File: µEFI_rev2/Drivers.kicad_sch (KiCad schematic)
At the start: 28 parts, among them Q1 ISL9V5045S3ST, Q2 ISL9V5045S3ST, Q3 ISL9V5045S3ST, Q4 ISL9V5045S3ST

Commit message: uEFI v2 beta release
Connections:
- net CONN_1 renamed M4
- net CONN_2 renamed L3
- net CONN_21 renamed M3
- net CONN_22 renamed L4
- net CONN_41 renamed L2
- net CONN_42 renamed M2
- net CONN_61 renamed L1
- net CONN_62 renamed M1
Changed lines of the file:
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@@
     (effects (font (size 1.27 1.27)) (justify right bottom))
   )
-  (global_label "CONN_62" (shape input) (at 90.17 59.69 0)
-    (effects (font (size 1.27 1.27)) (justify left))
-    (property "Intersheet References" "${INTERSHEET_REFS}" (id 0) (at 0 0 0)
-      (effects (font (size 1.27 1.27)) hide)
+  (global_label "M1" (shape input) (at 90.17 59.69 0)
+    (effects (font (size 0.889 0.889)) (justify left))
+    (property "Intersheet References" "${INTERSHEET_REFS}" (id 0) (at 93.7217 59.6345 0)
+      (effects (font (size 0.889 0.889)) (justify left) hide)
     )
   )
-  (global_label "CONN_42" (shape input) (at 90.17 85.09 0)
-    (effects (font (size 1.27 1.27)) (justify left))
-    (property "Intersheet References" "${INTERSHEET_REFS}" (id 0) (at 0 0 0)
-      (effects (font (size 1.27 1.27)) hide)
+  (global_label "M2" (shape input) (at 90.17 85.09 0)
+    (effects (font (size 0.889 0.889)) (justify left))
+    (property "Intersheet References" "${INTERSHEET_REFS}" (id 0) (at 93.7217 85.0345 0)
+      (effects (font (size 0.889 0.889)) (justify left) hide)
     )
   )
-  (global_label "CONN_61" (shape input) (at 90.17 110.49 0)
-    (effects (font (size 1.27 1.27)) (justify left))
-    (property "Intersheet References" "${INTERSHEET_REFS}" (id 0) (at 0 0 0)
-      (effects (font (size 1.27 1.27)) hide)
+  (global_label "L1" (shape input) (at 90.17 110.49 0)
+    (effects (font (size 0.889 0.889)) (justify left))
+    (property "Intersheet References" "${INTERSHEET_REFS}" (id 0) (at 93.4253 110.4345 0)
+      (effects (font (size 0.889 0.889)) (justify left) hide)
     )
   )
-  (global_label "CONN_41" (shape input) (at 90.17 134.62 0)
-    (effects (font (size 1.27 1.27)) (justify left))
-    (property "Intersheet References" "${INTERSHEET_REFS}" (id 0) (at 0 0 0)
-      (effects (font (size 1.27 1.27)) hide)
+  (global_label "L2" (shape input) (at 90.17 134.62 0)
+    (effects (font (size 0.889 0.889)) (justify left))
+    (property "Intersheet References" "${INTERSHEET_REFS}" (id 0) (at 93.4253 134.5645 0)
+      (effects (font (size 0.889 0.889)) (justify left) hide)
     )
   )
-  (global_label "CONN_21" (shape input) (at 165.1 147.32 0)
+  (global_label "M3" (shape input) (at 165.1 147.32 0)
     (effects (font (size 1.27 1.27)) (justify left))
-    (property "Intersheet References" "${INTERSHEET_REFS}" (id 0) (at 0 0 0)
-      (effects (font (size 1.27 1.27)) hide)
+    (property "Intersheet References" "${INTERSHEET_REFS}" (id 0) (at 170.1741 147.2406 0)
+      (effects (font (size 1.27 1.27)) (justify left) hide)
     )
   )
-  (global_label "CONN_1" (shape input) (at 165.1 149.86 0)
+  (global_label "M4" (shape input) (at 165.1 149.86 0)
     (effects (font (size 1.27 1.27)) (justify left))
-    (property "Intersheet References" "${INTERSHEET_REFS}" (id 0) (at 0 0 0)
-      (effects (font (size 1.27 1.27)) hide)
+    (property "Intersheet References" "${INTERSHEET_REFS}" (id 0) (at 170.1741 149.7806 0)
+      (effects (font (size 1.27 1.27)) (justify left) hide)
     )
   )
-  (global_label "CONN_2" (shape input) (at 165.1 152.4 0)
+  (global_label "L3" (shape input) (at 165.1 152.4 0)
     (effects (font (size 1.27 1.27)) (justify left))
-    (property "Intersheet References" "${INTERSHEET_REFS}" (id 0) (at 0 0 0)
-      (effects (font (size 1.27 1.27)) hide)
+    (property "Intersheet References" "${INTERSHEET_REFS}" (id 0) (at 169.7507 152.3206 0)
+      (effects (font (size 1.27 1.27)) (justify left) hide)
     )
   )
-  (global_label "CONN_22" (shape input) (at 165.1 154.94 0)
+  (global_label "L4" (shape input) (at 165.1 154.94 0)
     (effects (font (size 1.27 1.27)) (justify left))
-    (property "Intersheet References" "${INTERSHEET_REFS}" (id 0) (at 0 0 0)
-      (effects (font (size 1.27 1.27)) hide)
+    (property "Intersheet References" "${INTERSHEET_REFS}" (id 0) (at 169.7507 154.8606 0)
+      (effects (font (size 1.27 1.27)) (justify left) hide)
     )
   )

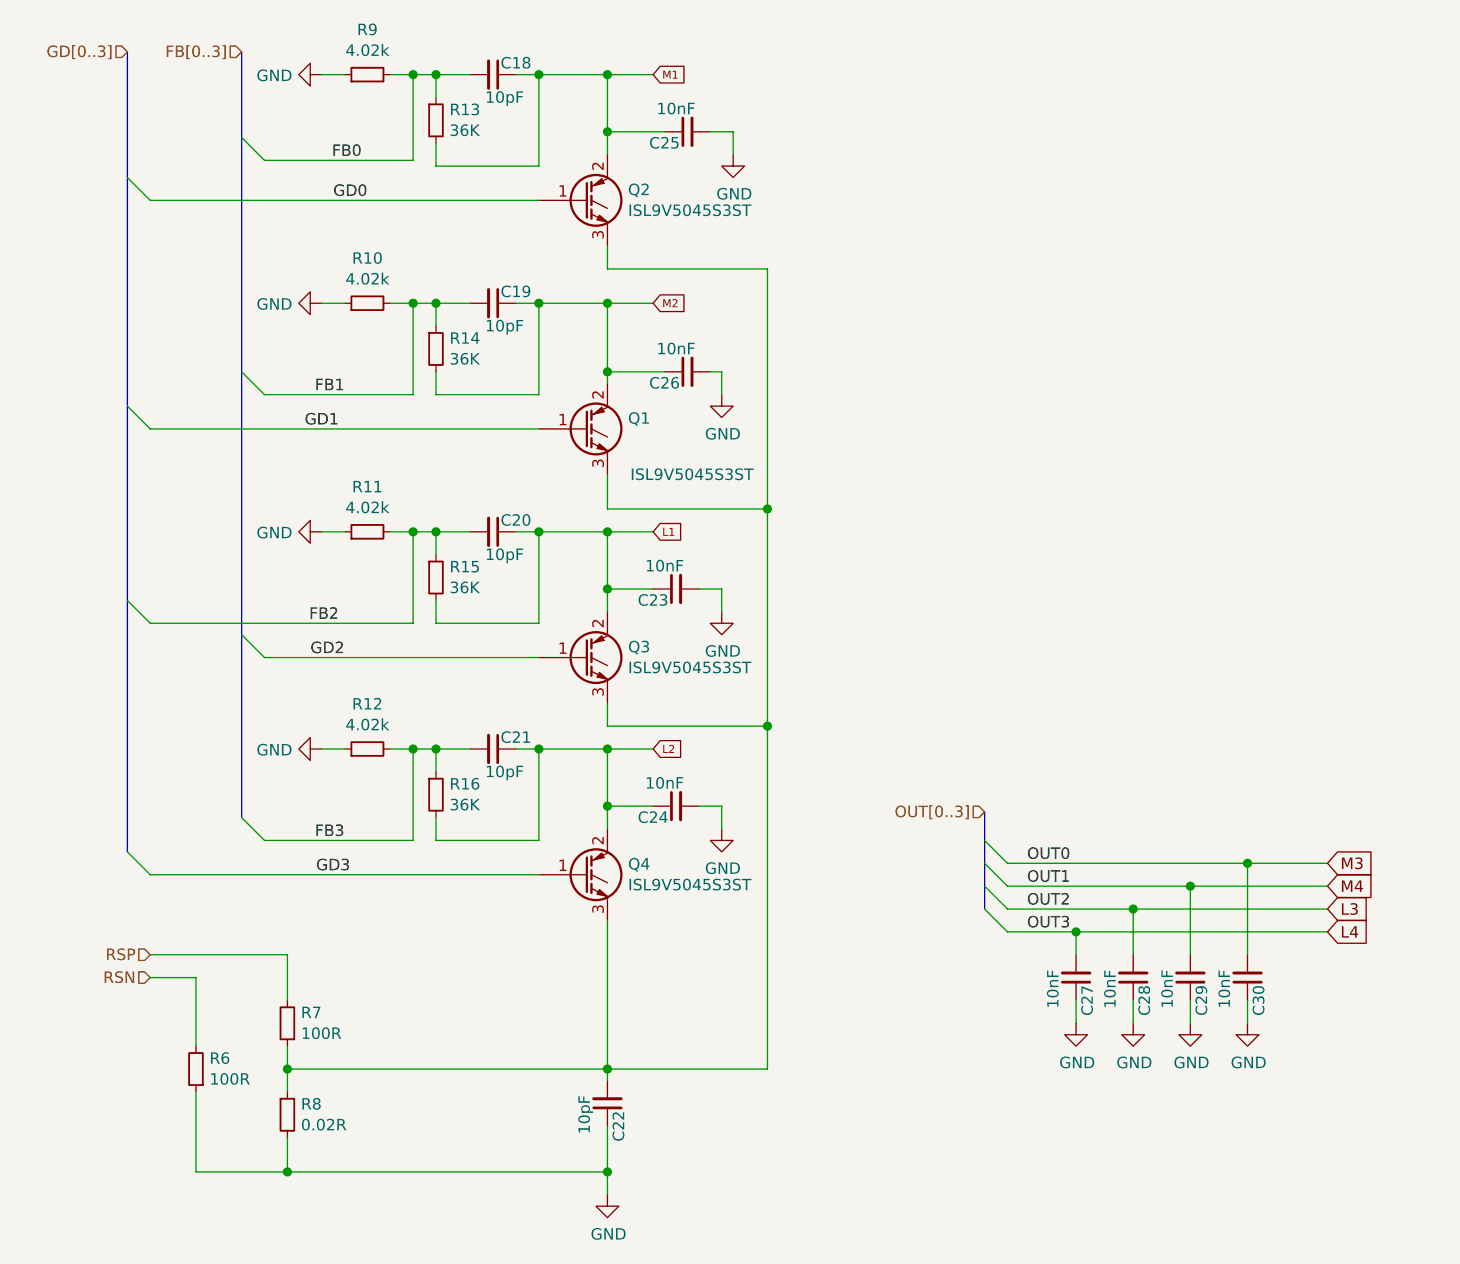
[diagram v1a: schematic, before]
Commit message: bump to kicad 6, init uEFI v3
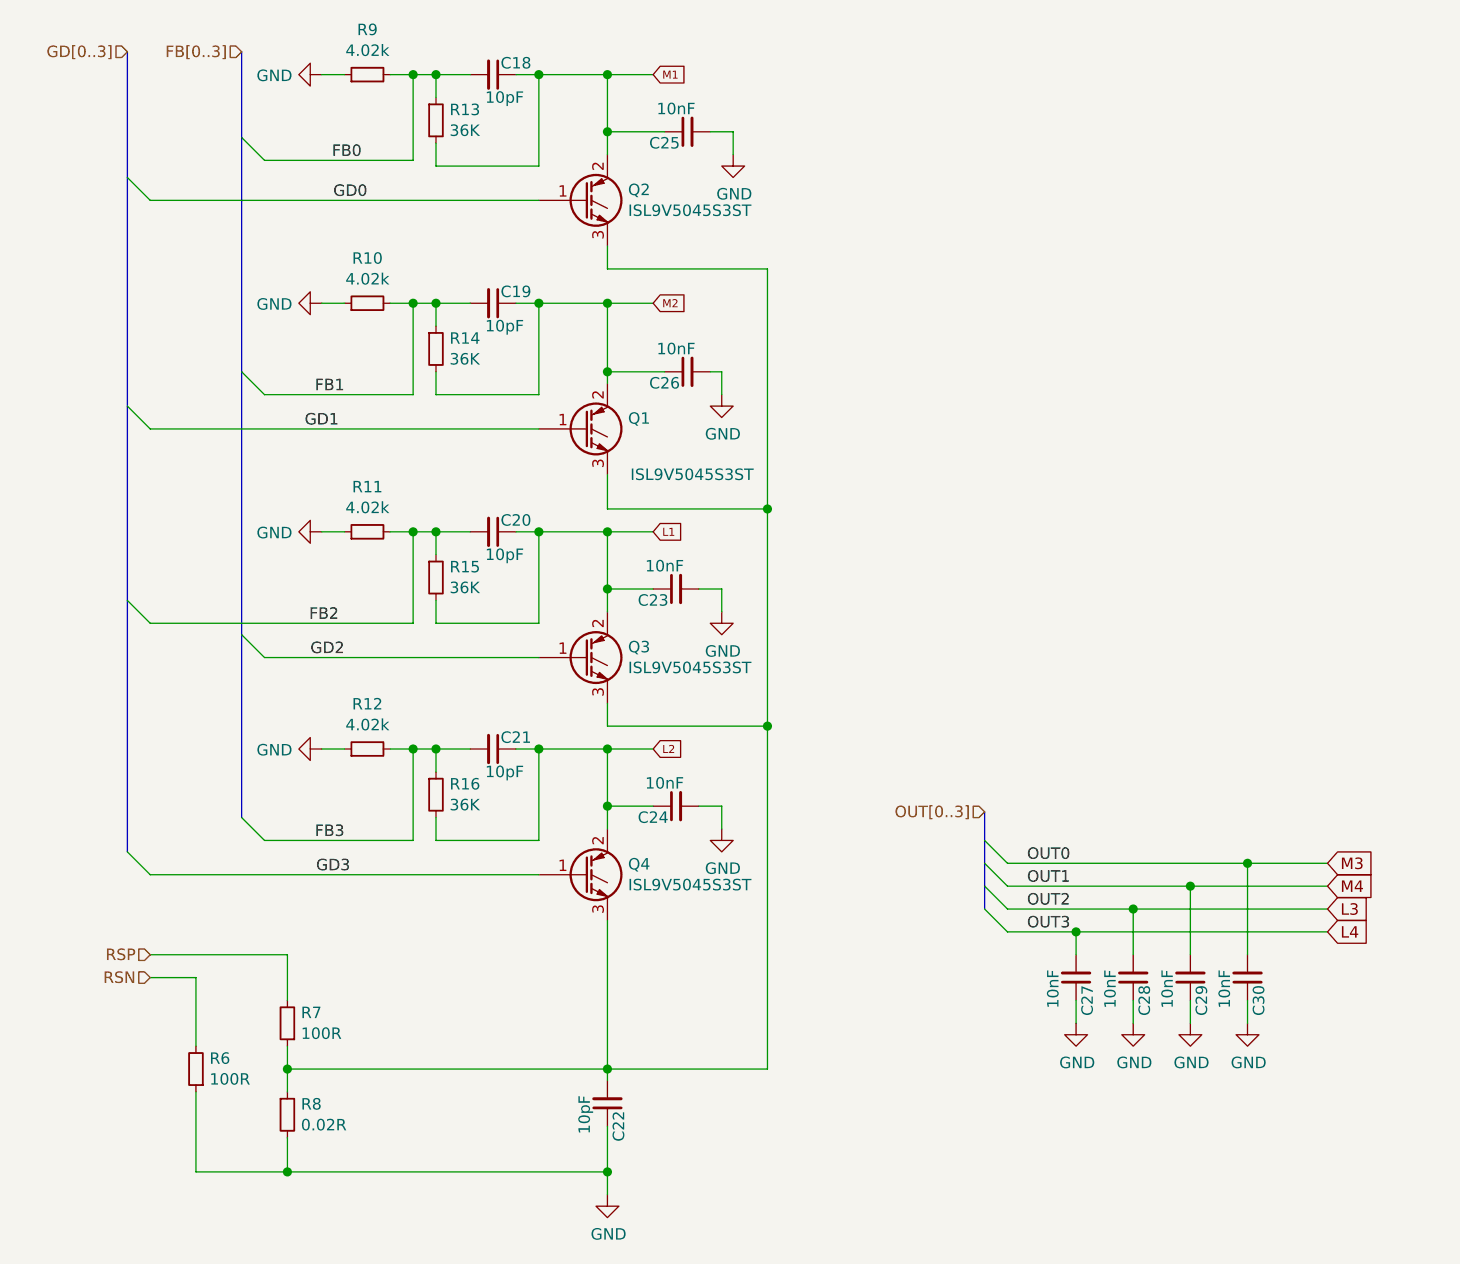
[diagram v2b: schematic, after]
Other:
- company: (none) -> Churrosoft
- title: (none) -> uEFI

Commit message: move old boards to __old
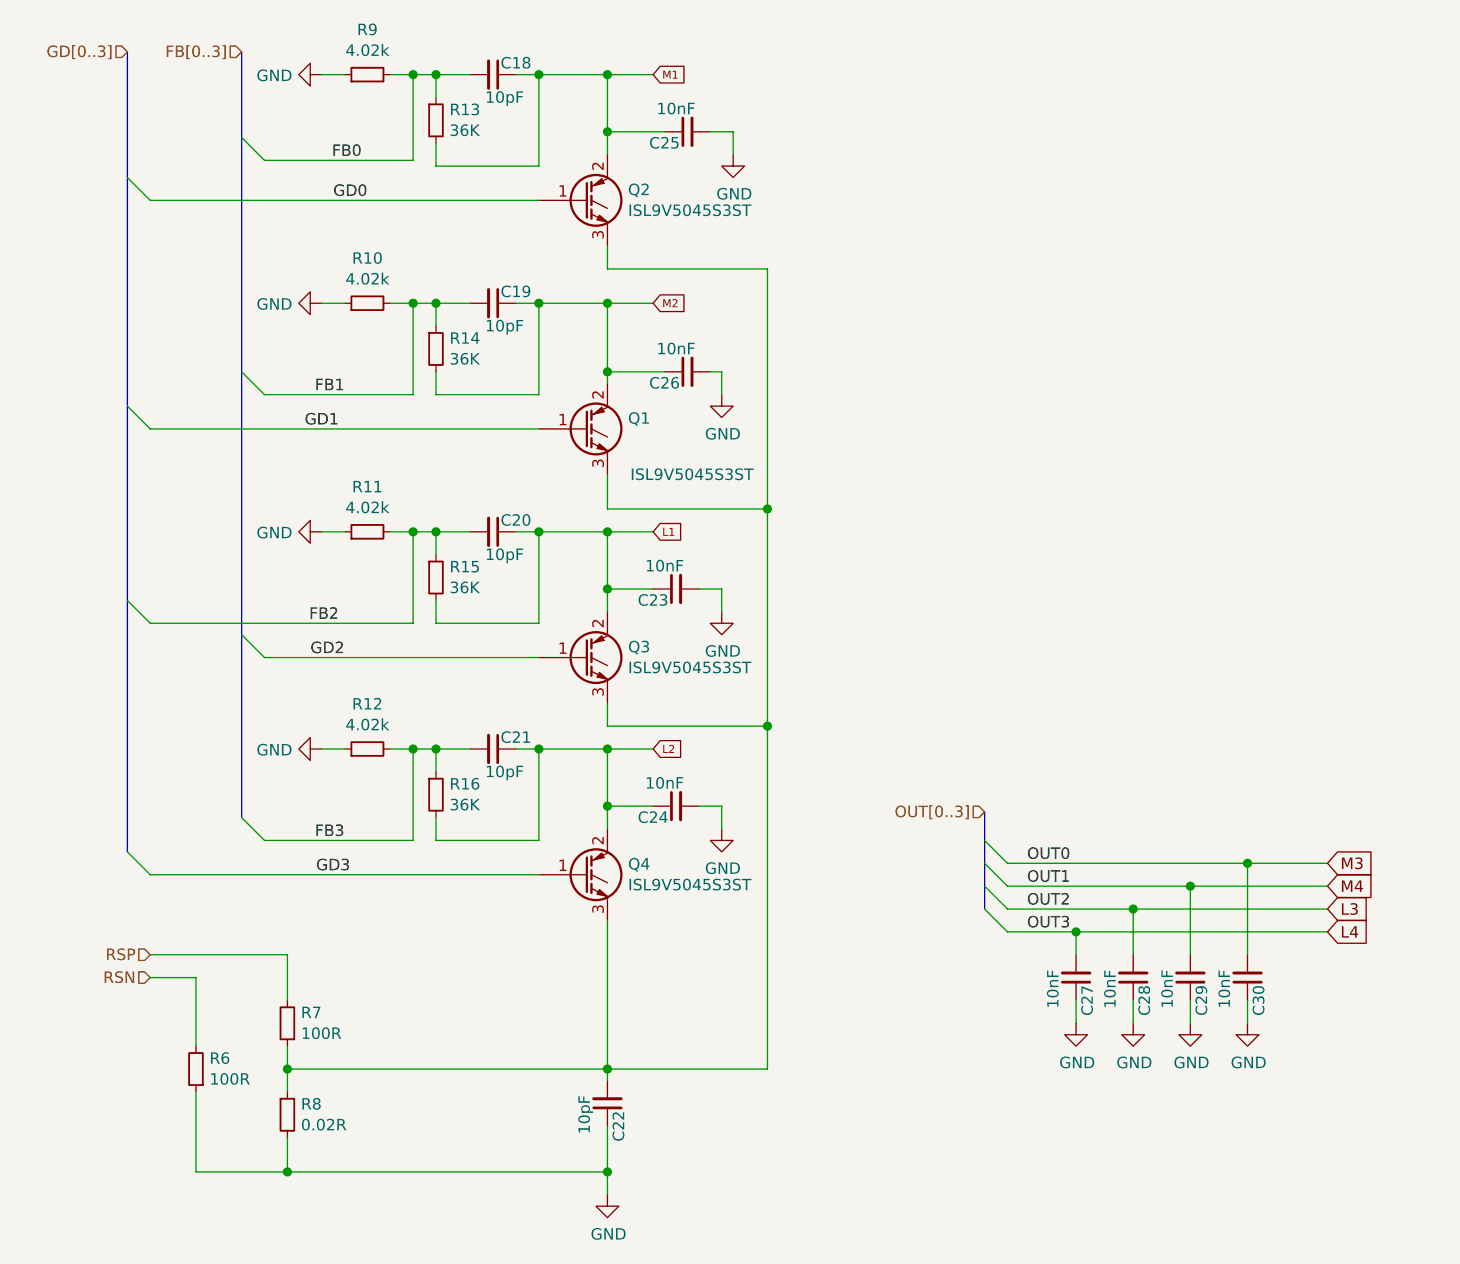
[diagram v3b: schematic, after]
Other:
- company: Churrosoft -> (none)
- title: uEFI -> (none)
